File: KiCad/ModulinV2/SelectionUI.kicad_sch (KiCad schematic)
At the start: 24 parts, among them IC33 CD4028BM96, IC36 E-ULN2003D1013TR, IC37 E-ULN2003D1013TR, IC38 CD4028BM96

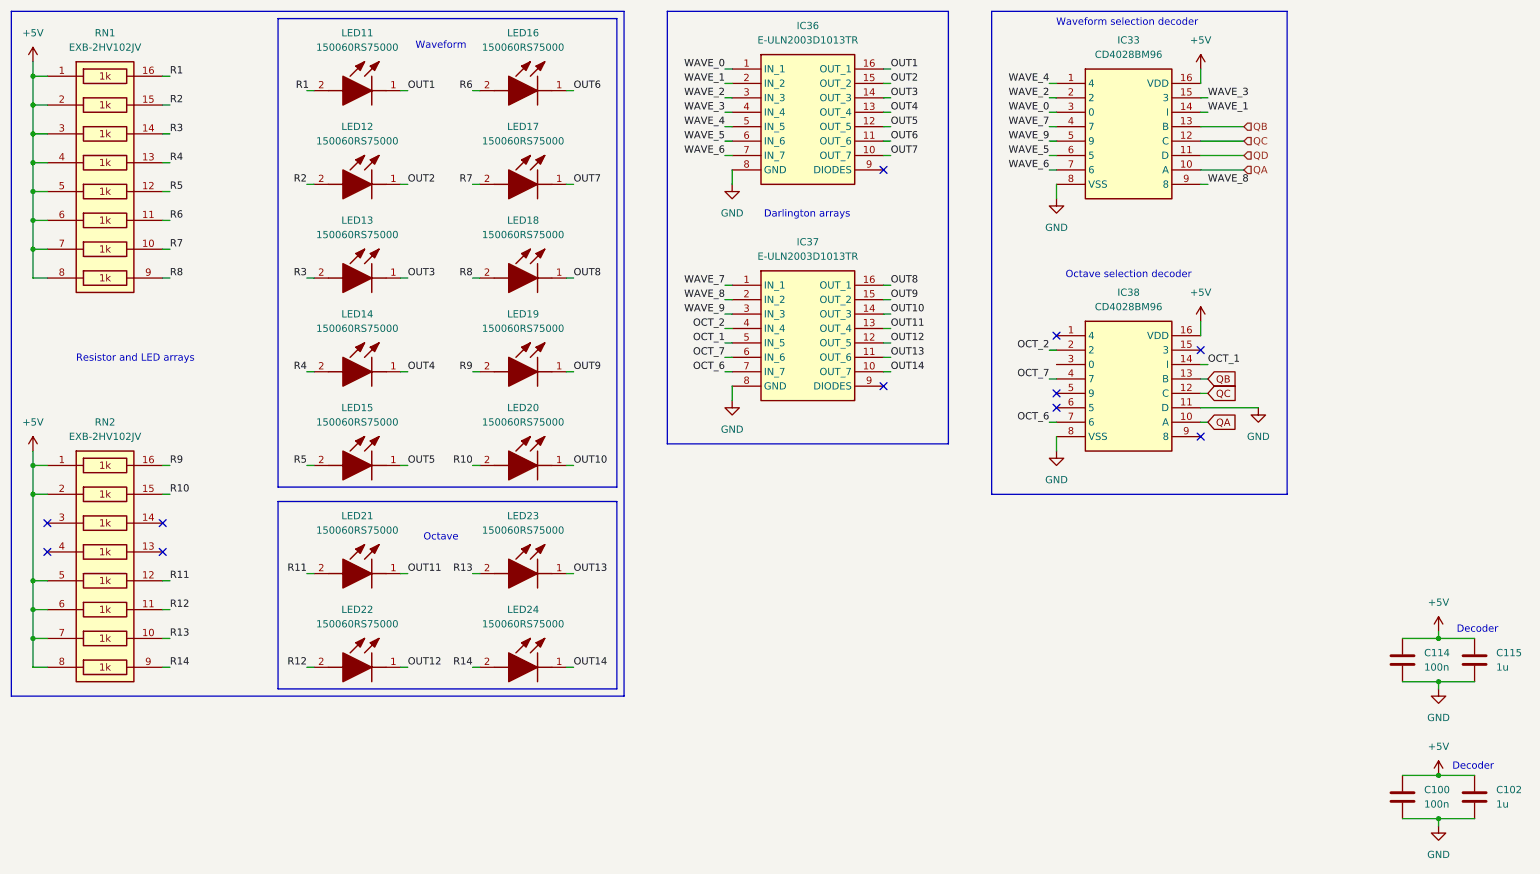
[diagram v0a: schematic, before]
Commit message: Fixed library issues and assigned most footprints
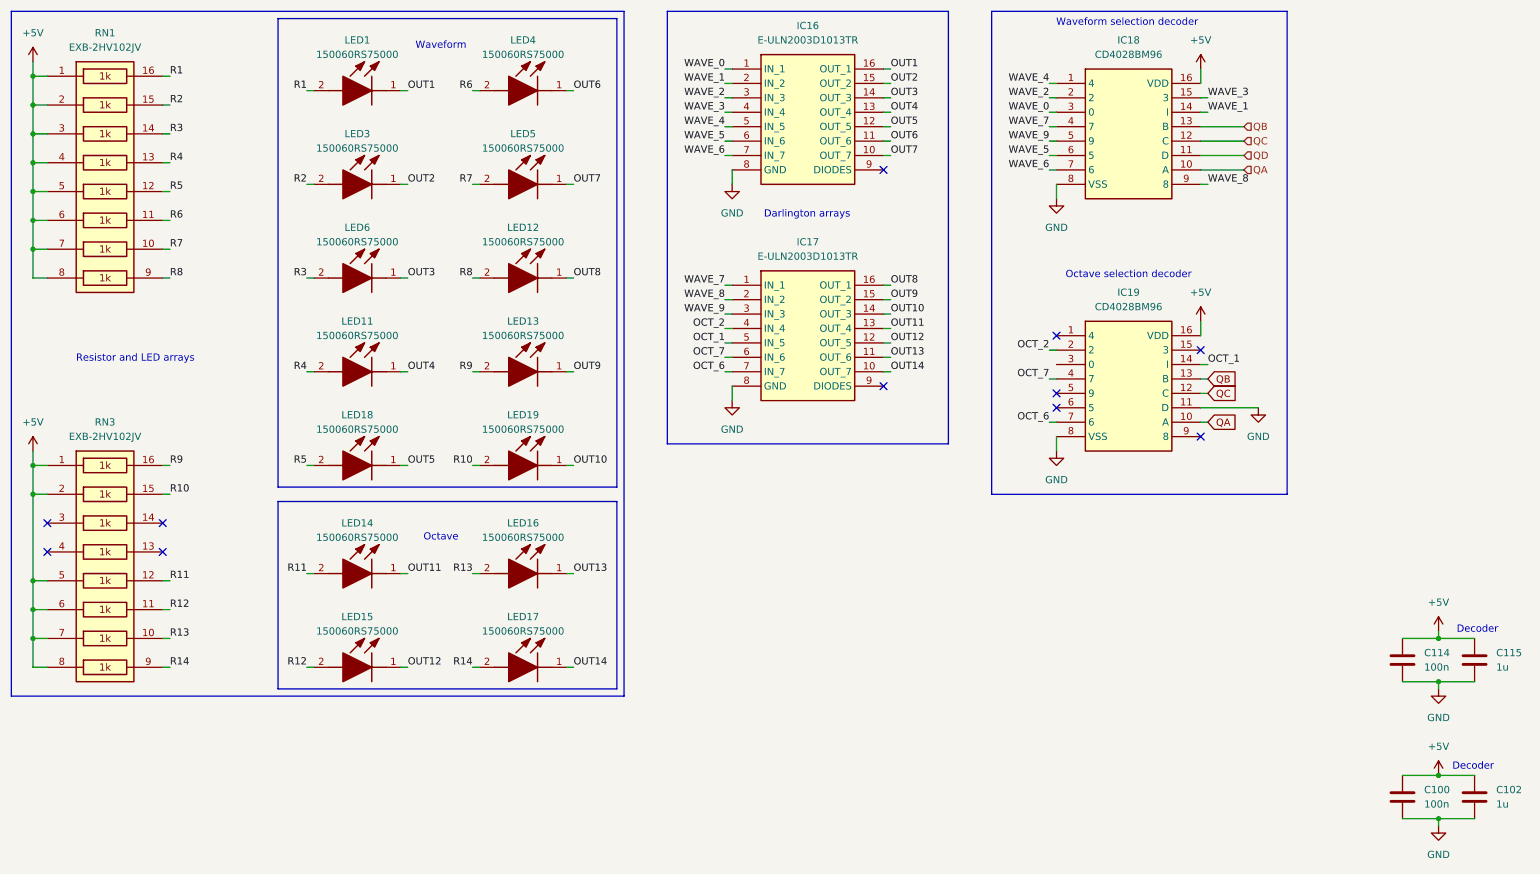
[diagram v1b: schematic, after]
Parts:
- removed IC33, IC38: CD4028BM96, SOIC127P600X175-16N, symbol CD4028BM96:CD4028BM96
- removed IC36, IC37: E-ULN2003D1013TR, SOIC127P600X175-16N, symbol E-ULN2003D1013TR:E-ULN2003D1013TR
- removed LED11, LED12, LED13, LED14, LED15, LED16, LED17, LED18, LED19, LED20, LED21, LED22, LED23, LED24: 150060RS75000, LEDC1608X80N, symbol 150060RS75000:150060RS75000
- removed RN1, RN2: EXB-2HV102JV, EXB2HV102JV, symbol EXB-2HV102JV:EXB-2HV102JV
- added IC16, IC17: E-ULN2003D1013TR, SamacSys_Parts:SOIC127P600X175-16N, symbol SamacSys_Parts:E-ULN2003D1013TR
- added IC18, IC19: CD4028BM96, SamacSys_Parts:SOIC127P600X175-16N, symbol SamacSys_Parts:CD4028BM96
- added LED1, LED11, LED12, LED13, LED14, LED15, LED16, LED17, LED18, LED19, LED3, LED4, LED5, LED6: 150060RS75000, SamacSys_Parts:LEDC1608X80N, symbol SamacSys_Parts:150060RS75000
- added RN1, RN3: EXB-2HV102JV, SamacSys_Parts:EXB2HV102JV, symbol SamacSys_Parts:EXB-2HV102JV
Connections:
- net +5V: now also IC18.16 (VDD), IC19.16 (VDD), RN1.1, RN1.2, RN1.3, RN1.4, RN1.5, RN1.6, RN1.7, RN1.8, RN3.1, RN3.2, RN3.5, RN3.6, RN3.7, RN3.8
- net GND: now also IC16.8 (GND), IC17.8 (GND), IC18.8 (VSS), IC19.11 (D), IC19.8 (VSS)
- net OCT_1: now also IC17.5 (IN_5), IC19.14 (I)
- net OCT_2: now also IC17.4 (IN_4), IC19.2
- net OCT_6: now also IC17.7 (IN_7), IC19.7 (6)
- net OCT_7: now also IC17.6 (IN_6), IC19.4 (7)
- net OUT1: now also IC16.16 (OUT_1), LED1.1 (K)
- net OUT10: now also IC17.14 (OUT_3), LED19.1 (K)
- net OUT11: now also IC17.13 (OUT_4), LED14.1 (K)
- net OUT12: now also IC17.12 (OUT_5), LED15.1 (K)
- net OUT13: now also IC17.11 (OUT_6), LED16.1 (K)
- net OUT14: now also IC17.10 (OUT_7), LED17.1 (K)
- net OUT2: now also IC16.15 (OUT_2), LED3.1 (K)
- net OUT3: now also IC16.14 (OUT_3), LED6.1 (K)
- net OUT4: now also IC16.13 (OUT_4), LED11.1 (K)
- net OUT5: now also IC16.12 (OUT_5), LED18.1 (K)
- net OUT6: now also IC16.11 (OUT_6), LED4.1 (K)
- net OUT7: now also IC16.10 (OUT_7), LED5.1 (K)
- net OUT8: now also IC17.16 (OUT_1), LED12.1 (K)
- net OUT9: now also IC17.15 (OUT_2), LED13.1 (K)
- net QA: now also IC18.10 (A), IC19.10 (A)
- net QB: now also IC18.13 (B), IC19.13 (B)
- net QC: now also IC18.12 (C), IC19.12 (C)
- net QD: now also IC18.11 (D)
- net R1: now also LED1.2 (A), RN1.16
- net R10: now also LED19.2 (A), RN3.15
- net R11: now also LED14.2 (A), RN3.12
- net R12: now also LED15.2 (A), RN3.11
- net R13: now also LED16.2 (A), RN3.10
- net R14: now also LED17.2 (A), RN3.9
- net R2: now also LED3.2 (A), RN1.15
- net R3: now also LED6.2 (A), RN1.14
- net R4: now also LED11.2 (A), RN1.13
- net R5: now also LED18.2 (A), RN1.12
- net R6: now also LED4.2 (A), RN1.11
- net R7: now also LED5.2 (A), RN1.10
- net R8: now also LED12.2 (A), RN1.9
- net R9: now also LED13.2 (A), RN3.16
- net WAVE_0: now also IC16.1 (IN_1), IC18.3 (0)
- net WAVE_1: now also IC16.2 (IN_2), IC18.14 (I)
- net WAVE_2: now also IC16.3 (IN_3), IC18.2
- net WAVE_3: now also IC16.4 (IN_4), IC18.15 (3)
- net WAVE_4: now also IC16.5 (IN_5), IC18.1 (4)
- net WAVE_5: now also IC16.6 (IN_6), IC18.6 (5)
- net WAVE_6: now also IC16.7 (IN_7), IC18.7 (6)
- net WAVE_7: now also IC17.1 (IN_1), IC18.4 (7)
- net WAVE_8: now also IC17.2 (IN_2), IC18.9 (8)
- net WAVE_9: now also IC17.3 (IN_3), IC18.5 (9)
